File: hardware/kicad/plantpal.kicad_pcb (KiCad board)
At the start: 2 copper layers, 38.4 x 128.5 mm, 123 parts, among them J1 U262-161N-4BVC11, J2 +LIPO, J3 -LIPO, J4 687124182122, Q1 DMG1012UW, Q2 DMG3415U-7, Q3 MMBT3906, Q4 PMV32UP, Q5 DMG1012UW, Q6 AO3407A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

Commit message: update 3d model
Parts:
- D7, D8: footprint Diode_SMD:D_0402_1005Metric -> plantpal:D_0402_1005Metric
- Q8: footprint Package_TO_SOT_SMD:SOT-883 -> plantpal:SOT-883
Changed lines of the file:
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@@
     (property "ki_keywords" "capacitor cap")
     (attr smd)
-    (fp_text reference "C25" (at 1.755 -0.24 90) (layer "F.Fab")
+    (fp_text reference "C25" (at 1.505 0.29 90) (layer "F.Fab")
         (effects (font (size 0.3 0.3) (thickness 0.075) bold))
     )
@@
       (net 43 "Net-(J2-Pin_1)") (pinfunction "Pin_1") (pintype "passive"))
   )
-  (footprint "Package_TO_SOT_SMD:SOT-883" (layer "F.Cu")
+  (footprint "plantpal:SOT-883" (layer "F.Cu")
     (at 117.53 56.215 180)
     (descr "SOT-883, https://assets.nexperia.com/documents/outline-drawing/SOT883.pdf")
@@
     (property "ki_keywords" "transistor PMOS P-MOS P-MOSFET")
     (attr smd)
-    (fp_text reference "Q8" (at 0 -1.905) (layer "F.Fab")
+    (fp_text reference "Q8" (at -0.09 0.795 180) (layer "F.Fab")
         (effects (font (size 0.3 0.3) (thickness 0.075)))
     )
-    (fp_text value "PMZ350UPEYL" (at 0 1.905) (layer "F.Fab")
+    (fp_text value "PMZ350UPEYL" (at -2.16 0.895 180) (layer "F.Fab")
         (effects (font (size 0.3 0.3) (thickness 0.075)))
     )
-    (fp_text user "${REFERENCE}" (at 0 0) (layer "F.Fab")
+    (fp_text user "${REFERENCE}" (at 0 0 180) (layer "F.Fab")
         (effects (font (size 0.2 0.2) (thickness 0.03)))
     )
@@
     (pad "3" smd roundrect (at 0.35 0 180) (size 0.4 0.7) (layers "F.Cu" "F.Paste" "F.Mask") (roundrect_rratio 0.125)
       (net 89 "Net-(Q8-D)") (pinfunction "D") (pintype "passive"))
-    (model "${KICAD6_3DMODEL_DIR}/Package_TO_SOT_SMD.3dshapes/SOT-883.wrl"
+    (model "${KIPRJMOD}/library/3dmodels/X1-DFN1006-3_L1.0-W0.6-H0.5-P0.35-BR.wrl"
       (offset (xyz 0 0 0))
       (scale (xyz 1 1 1))
-      (rotate (xyz 0 0 0))
+      (rotate (xyz 0 0 180))
     )
   )
@@
     )
   )
-  (footprint "Diode_SMD:D_0402_1005Metric" (layer "F.Cu")
+  (footprint "plantpal:D_0402_1005Metric" (layer "F.Cu")
     (at 125.7825 37.06 180)
     (descr "Diode SMD 0402 (1005 Metric), square (rectangular) end terminal, IPC_7351 nominal, (Body size source: http://www.tortai-tech.com/upload/download/2011102023233369053.pdf), generated with kicad-footprint-generator")
@@
     (property "ki_keywords" "diode Schottky")
     (attr smd)
-    (fp_text reference "D8" (at 0 -1.17) (layer "F.Fab")
+    (fp_text reference "D8" (at -1.3475 -0.08 180) (layer "F.Fab")
         (effects (font (size 0.3 0.3) (thickness 0.075)))
     )
-    (fp_text value "RB161QS-40T18R" (at 0 1.17) (layer "F.Fab")
+    (fp_text value "RB161QS-40T18R" (at -0.9675 0.69 180) (layer "F.Fab")
         (effects (font (size 0.3 0.3) (thickness 0.075)))
     )
-    (fp_text user "${REFERENCE}" (at 0 0) (layer "F.Fab")
+    (fp_text user "${REFERENCE}" (at 0 0 180) (layer "F.Fab")
         (effects (font (size 0.25 0.25) (thickness 0.04)))
     )
@@
     (pad "2" smd roundrect (at 0.485 0 180) (size 0.59 0.64) (layers "F.Cu" "F.Paste" "F.Mask") (roundrect_rratio 0.25)
       (net 11 "/Main Controller/CHIP_EN") (pinfunction "A") (pintype "passive"))
-    (model "${KICAD6_3DMODEL_DIR}/Diode_SMD.3dshapes/D_0402_1005Metric.wrl"
+    (model "${KIPRJMOD}/library/3dmodels/X2-DFN1006-2_L1.0-W0.6-H0.4-P0.65-RD.wrl"
       (offset (xyz 0 0 0))
       (scale (xyz 1 1 1))
@@
     (property "ki_keywords" "R resistor")
     (attr smd)
-    (fp_text reference "R8" (at 0.81 0 90) (layer "F.Fab")
+    (fp_text reference "R8" (at 0.89 0.795 90) (layer "F.Fab")
         (effects (font (size 0.3 0.3) (thickness 0.075)))
     )
@@
     (property "ki_keywords" "R resistor")
     (attr smd)
-    (fp_text reference "R14" (at 0.06 -0.93 90) (layer "F.Fab")
+    (fp_text reference "R14" (at 0.23 -0.76 180) (layer "F.Fab")
         (effects (font (size 0.3 0.3) (thickness 0.075)))
     )
-    (fp_text value "16K9" (at 0.47 -0.93 90) (layer "F.Fab")
+    (fp_text value "16K9" (at 1.1 -1.59 -90) (layer "F.Fab")
         (effects (font (size 0.3 0.3) (thickness 0.075)))
     )
@@
     (property "ki_keywords" "capacitor cap")
     (attr smd)
-    (fp_text reference "C26" (at 1.735 0.24 90) (layer "F.Fab")
+    (fp_text reference "C26" (at -1.135 -0.7 180) (layer "F.Fab")
         (effects (font (size 0.3 0.3) (thickness 0.075)))
     )
-    (fp_text value "10u" (at 1.965 -0.57) (layer "F.Fab")
+    (fp_text value "10u" (at -1.105 0.99) (layer "F.Fab")
         (effects (font (size 0.3 0.3) (thickness 0.075)))
     )
@@
         (effects (font (size 0.3 0.3) (thickness 0.075)))
     )
-    (fp_text value "10K" (at 0 1.17) (layer "F.Fab")
+    (fp_text value "10K" (at -0.9 -0.72) (layer "F.Fab")
         (effects (font (size 0.3 0.3) (thickness 0.075)))
     )
@@
     (property "ki_keywords" "capacitor cap")
     (attr smd)
-    (fp_text reference "C13" (at -0.82 0 90) (layer "F.Fab")
+    (fp_text reference "C13" (at 0.48 0.675 180) (layer "F.Fab")
         (effects (font (size 0.3 0.3) (thickness 0.075)))
     )
@@
     (property "ki_keywords" "R resistor")
     (attr smd)
-    (fp_text reference "R28" (at 0 -1.17 90) (layer "F.Fab")
+    (fp_text reference "R28" (at -1.24 0.06 180) (layer "F.Fab")
         (effects (font (size 0.3 0.3) (thickness 0.075)))
     )
@@
     )
   )
-  (footprint "Diode_SMD:D_0402_1005Metric" (layer "F.Cu")
+  (footprint "plantpal:D_0402_1005Metric" (layer "F.Cu")
     (at 109.81 47.61 90)
     (descr "Diode SMD 0402 (1005 Metric), square (rectangular) end terminal, IPC_7351 nominal, (Body size source: http://www.tortai-tech.com/upload/download/2011102023233369053.pdf), generated with kicad-footprint-generator")
@@
     (property "ki_keywords" "diode Schottky")
     (attr smd)
-    (fp_text reference "D7" (at 0.74 0.8 180) (layer "F.Fab")
+    (fp_text reference "D7" (at 1.19 -0.35 180) (layer "F.Fab")
         (effects (font (size 0.3 0.3) (thickness 0.075)))
     )
-    (fp_text value "RB161QS-40T18R" (at 0.73 -0.61 270) (layer "F.Fab")
+    (fp_text value "RB161QS-40T18R" (at 0.77 2.67 180) (layer "F.Fab")
         (effects (font (size 0.3 0.3) (thickness 0.075)))
     )
@@
     (pad "2" smd roundrect (at 0.485 0 90) (size 0.59 0.64) (layers "F.Cu" "F.Paste" "F.Mask") (roundrect_rratio 0.25)
       (net 91 "/Main Controller/M_DRVOUT") (pinfunction "A") (pintype "passive"))
-    (model "${KICAD6_3DMODEL_DIR}/Diode_SMD.3dshapes/D_0402_1005Metric.wrl"
+    (model "${KIPRJMOD}/library/3dmodels/X2-DFN1006-2_L1.0-W0.6-H0.4-P0.65-RD.wrl"
       (offset (xyz 0 0 0))
       (scale (xyz 1 1 1))
@@
     (property "ki_keywords" "R resistor")
     (attr smd)
-    (fp_text reference "R9" (at 1.74 -0.355 180) (layer "F.Fab")
+    (fp_text reference "R9" (at 1.21 -0.095 -90) (layer "F.Fab")
         (effects (font (size 0.3 0.3) (thickness 0.075)))
     )

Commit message: wip
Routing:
- net /Main Controller/PWR_STATUS: track 8.65 -> 10.5 mm
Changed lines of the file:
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@@
   (via (at 127.92 60.15) (size 0.6) (drill 0.3) (layers "F.Cu" "B.Cu") (free) (net 2))
   (via (at 121.94 70.05) (size 0.6) (drill 0.3) (layers "F.Cu" "B.Cu") (free) (net 2))
-  (via (at 95.61 59.67) (size 0.6) (drill 0.3) (layers "F.Cu" "B.Cu") (free) (net 2))
+  (via (at 96.8 59.79) (size 0.6) (drill 0.3) (layers "F.Cu" "B.Cu") (free) (net 2))
   (via (at 100.96 70.08) (size 0.6) (drill 0.3) (layers "F.Cu" "B.Cu") (free) (net 2))
   (via (at 126.1 36.16) (size 0.6) (drill 0.3) (layers "F.Cu" "B.Cu") (free) (net 2))
@@
   (via (at 117.23 44.9) (size 0.6) (drill 0.3) (layers "F.Cu" "B.Cu") (net 2))
   (via (at 92.39 41.51) (size 0.6) (drill 0.3) (layers "F.Cu" "B.Cu") (free) (net 2))
+  (via (at 118.4 61.09) (size 0.6) (drill 0.3) (layers "F.Cu" "B.Cu") (free) (net 2))
   (via (at 100.93 67.63) (size 0.6) (drill 0.3) (layers "F.Cu" "B.Cu") (free) (net 2))
   (via (at 91.36 67.94) (size 0.6) (drill 0.3) (layers "F.Cu" "B.Cu") (free) (net 2))
@@
   (via (at 119.94 38.67) (size 0.6) (drill 0.3) (layers "F.Cu" "B.Cu") (free) (net 2))
   (via (at 116.26 47.86) (size 0.6) (drill 0.3) (layers "F.Cu" "B.Cu") (free) (net 2))
-  (via (at 97.96 60.7) (size 0.6) (drill 0.3) (layers "F.Cu" "B.Cu") (free) (net 2))
   (segment (start 115.505899 38.754) (end 115.503 38.754) (width 0.25) (layer "F.Cu") (net 4))
   (segment (start 113.92 37.845) (end 113.92 38.47) (width 0.6) (layer "F.Cu") (net 4))
@@
   (via (at 114.5 55.1) (size 0.6) (drill 0.3) (layers "F.Cu" "B.Cu") (net 58))
   (segment (start 110.01 54.9405) (end 110.01 56.451059) (width 0.25) (layer "B.Cu") (net 58))
+  (segment (start 112.6 53.39) (end 114.31 55.1) (width 0.25) (layer "B.Cu") (net 58))
+  (segment (start 110.54 53.39) (end 112.6 53.39) (width 0.25) (layer "B.Cu") (net 58))
+  (segment (start 110.01 53.92) (end 110.54 53.39) (width 0.25) (layer "B.Cu") (net 58))
   (segment (start 110.01 56.451059) (end 110.0095 56.451559) (width 0.25) (layer "B.Cu") (net 58))
-  (segment (start 110.1695 55.1) (end 110.01 54.9405) (width 0.25) (layer "B.Cu") (net 58))
-  (segment (start 114.5 55.1) (end 110.1695 55.1) (width 0.25) (layer "B.Cu") (net 58))
+  (segment (start 110.01 54.9405) (end 110.01 53.92) (width 0.25) (layer "B.Cu") (net 58))
+  (segment (start 114.31 55.1) (end 114.5 55.1) (width 0.25) (layer "B.Cu") (net 58))
   (segment (start 116.205 45.324) (end 116.196398 45.315398) (width 0.25) (layer "F.Cu") (net 59))
   (segment (start 115.28 52.14) (end 115.28 51.47) (width 0.5) (layer "F.Cu") (net 59))

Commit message: wip
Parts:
- moved C20 0.37 mm to (98.7, 51.9)
- moved R13 0.34 mm to (98.5, 49.9)
- turned D1 to 90 degrees
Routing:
- net +BATT: track 47.4 -> 46.6 mm
- net Net-(D1-K): track 6.70 -> 7.42 mm
- net GND: vias 188 -> 186

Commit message: wip
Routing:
- net GND: vias 186 -> 187
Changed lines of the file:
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@@
   (via (at 125.94 60.27) (size 0.6) (drill 0.3) (layers "F.Cu" "B.Cu") (free) (net 2))
   (via (at 111.44 39.17) (size 0.6) (drill 0.3) (layers "F.Cu" "B.Cu") (free) (net 2))
+  (via (at 99.83 48.17) (size 0.6) (drill 0.3) (layers "F.Cu" "B.Cu") (free) (net 2))
   (via (at 101.93 41.56) (size 0.6) (drill 0.3) (layers "F.Cu" "B.Cu") (free) (net 2))
   (via (at 110.96 40.55) (size 0.6) (drill 0.3) (layers "F.Cu" "B.Cu") (free) (net 2))

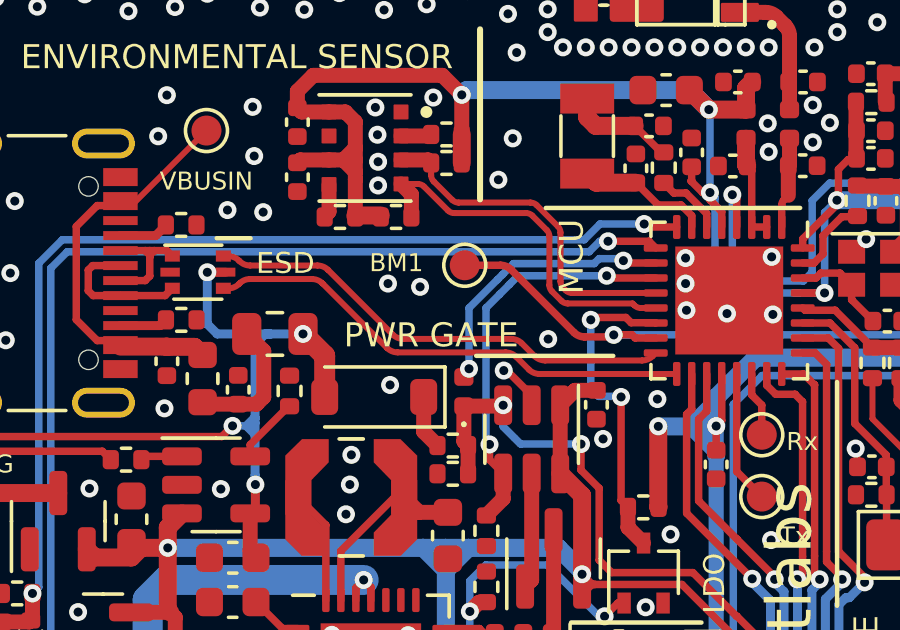
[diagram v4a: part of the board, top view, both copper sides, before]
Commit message: improve usb trace
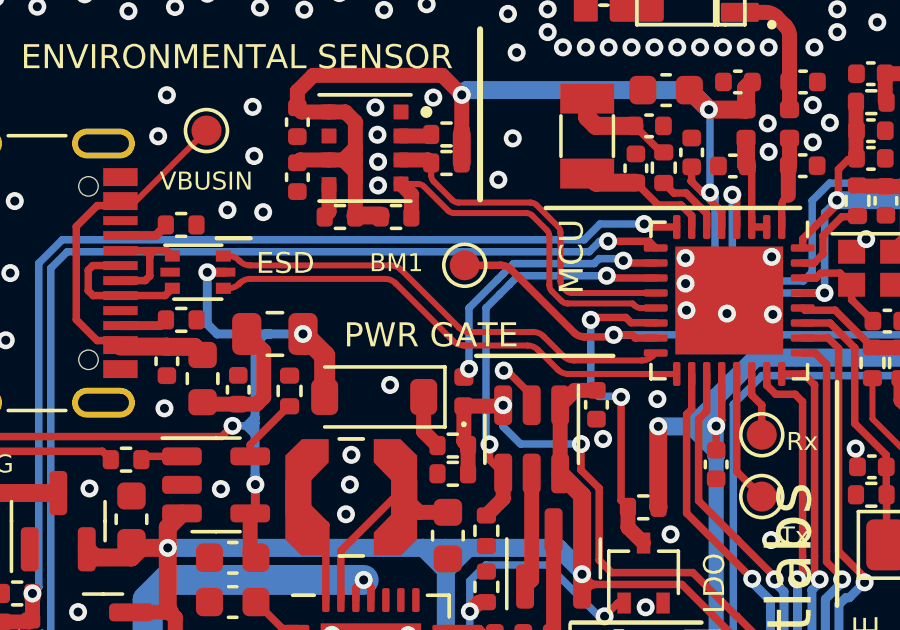
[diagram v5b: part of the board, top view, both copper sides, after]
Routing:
- net GND: vias 187 -> 184
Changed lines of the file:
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@@
   (via (at 128.03 67.67) (size 0.6) (drill 0.3) (layers "F.Cu" "B.Cu") (free) (net 2))
   (via (at 126.01 35.15) (size 0.6) (drill 0.3) (layers "F.Cu" "B.Cu") (free) (net 2))
-  (via (at 108.35 44.12) (size 0.6) (drill 0.3) (layers "F.Cu" "B.Cu") (free) (net 2))
   (via (at 97.88 71.55) (size 0.6) (drill 0.3) (layers "F.Cu" "B.Cu") (free) (net 2))
   (via (at 102.82 39.76) (size 0.6) (drill 0.3) (layers "F.Cu" "B.Cu") (free) (net 2))
@@
   (via (at 124.7 36.03) (size 0.6) (drill 0.3) (layers "F.Cu" "B.Cu") (free) (net 2))
   (via (at 126.27 72.15) (size 0.6) (drill 0.3) (layers "F.Cu" "B.Cu") (free) (net 2))
-  (via (at 112.62 45.86) (size 0.6) (drill 0.3) (layers "F.Cu" "B.Cu") (free) (net 2))
   (via (at 101.26 34.35) (size 0.6) (drill 0.3) (layers "F.Cu" "B.Cu") (free) (net 2))
   (via (at 98.09 65.78) (size 0.6) (drill 0.3) (layers "F.Cu" "B.Cu") (free) (net 2))
@@
   (via (at 102.19 33.67) (size 0.6) (drill 0.3) (layers "F.Cu" "B.Cu") (free) (net 2))
   (via (at 106.95 40.74) (size 0.6) (drill 0.3) (layers "F.Cu" "B.Cu") (free) (net 2))
-  (via (at 107.28 44.01) (size 0.6) (drill 0.3) (layers "F.Cu" "B.Cu") (free) (net 2))
   (via (at 92.46 34.42) (size 0.6) (drill 0.3) (layers "F.Cu" "B.Cu") (free) (net 2))
   (via (at 103.34 68.46) (size 0.6) (drill 0.3) (layers "F.Cu" "B.Cu") (free) (net 2))
@@
   (segment (start 119.74 48.06) (end 119.74 49.05) (width 0.25) (layer "F.Cu") (net 76))
   (segment (start 119.405 47.024) (end 119.405 47.725) (width 0.25) (layer "F.Cu") (net 76))
-  (segment (start 107.790307 45.855) (end 111.386093 45.855) (width 0.2) (layer "F.Cu") (net 77))
-  (segment (start 101.79 43.096) (end 101.957894 43.096) (width 0.2) (layer "F.Cu") (net 77))
-  (segment (start 112.519306 46.573999) (end 115.747894 46.573999) (width 0.2) (layer "F.Cu") (net 77))
-  (segment (start 102.684608 43.4085) (end 104.929593 43.4085) (width 0.2) (layer "F.Cu") (net 77))
+  (segment (start 102.687608 43.4045) (end 107.365593 43.4045) (width 0.2) (layer "F.Cu") (net 77))
+  (segment (start 112.469647 45.771447) (end 113.125753 46.427553) (width 0.2) (layer "F.Cu") (net 77))
+  (segment (start 113.479306 46.573999) (end 115.747894 46.573999) (width 0.2) (layer "F.Cu") (net 77))
+  (segment (start 110.000307 45.625) (end 112.116093 45.625) (width 0.2) (layer "F.Cu") (net 77))
+  (segment (start 101.793 43.092) (end 101.960894 43.092) (width 0.2) (layer "F.Cu") (net 77))
+  (segment (start 102.314448 43.238447) (end 102.334055 43.258054) (width 0.2) (layer "F.Cu") (net 77))
   (segment (start 116.101448 46.427552) (end 116.205 46.324) (width 0.2) (layer "F.Cu") (net 77))
-  (segment (start 111.739647 46.001447) (end 112.165753 46.427553) (width 0.2) (layer "F.Cu") (net 77))
-  (segment (start 105.283147 43.554947) (end 107.436754 45.708554) (width 0.2) (layer "F.Cu") (net 77))
-  (segment (start 102.311448 43.242447) (end 102.331055 43.262054) (width 0.2) (layer "F.Cu") (net 77))
-  (arc (start 102.684608 43.4085) (mid 102.493267 43.37044) (end 102.331055 43.262054) (width 0.2) (layer "F.Cu") (net 77))
-  (arc (start 101.957894 43.096) (mid 102.149236 43.13406) (end 102.311448 43.242447) (width 0.2) (layer "F.Cu") (net 77))
-  (arc (start 112.165753 46.427553) (mid 112.327965 46.535939) (end 112.519306 46.573999) (width 0.2) (layer "F.Cu") (net 77))
-  (arc (start 107.790307 45.855) (mid 107.598966 45.81694) (end 107.436754 45.708554) (width 0.2) (layer "F.Cu") (net 77))
-  (arc (start 111.386093 45.855) (mid 111.577435 45.89306) (end 111.739647 46.001447) (width 0.2) (layer "F.Cu") (net 77))
-  (arc (start 104.929593 43.4085) (mid 105.120935 43.44656) (end 105.283147 43.554947) (width 0.2) (layer "F.Cu") (net 77))
+  (segment (start 107.719147 43.550947) (end 109.646754 45.478554) (width 0.2) (layer "F.Cu") (net 77))
+  (arc (start 109.646754 45.478554) (mid 109.808966 45.58694) (end 110.000307 45.625) (width 0.2) (layer "F.Cu") (net 77))
+  (arc (start 102.334055 43.258054) (mid 102.496267 43.36644) (end 102.687608 43.4045) (width 0.2) (layer "F.Cu") (net 77))
   (arc (start 116.101448 46.427552) (mid 115.939236 46.535939) (end 115.747894 46.573999) (width 0.2) (layer "F.Cu") (net 77))
-  (segment (start 111.553247 46.451447) (end 111.979354 46.877554) (width 0.2) (layer "F.Cu") (net 78))
-  (segment (start 112.332907 47.024) (end 116.905 47.024) (width 0.2) (layer "F.Cu") (net 78))
-  (segment (start 101.79 44.171) (end 101.957894 44.171) (width 0.2) (layer "F.Cu") (net 78))
-  (segment (start 105.096747 44.004947) (end 107.250354 46.158554) (width 0.2) (layer "F.Cu") (net 78))
-  (segment (start 102.311448 44.024553) (end 102.331055 44.004946) (width 0.2) (layer "F.Cu") (net 78))
-  (segment (start 102.684608 43.8585) (end 104.743193 43.8585) (width 0.2) (layer "F.Cu") (net 78))
-  (segment (start 107.603907 46.305) (end 111.199693 46.305) (width 0.2) (layer "F.Cu") (net 78))
-  (arc (start 102.684608 43.8585) (mid 102.493267 43.89656) (end 102.331055 44.004946) (width 0.2) (layer "F.Cu") (net 78))
-  (arc (start 112.332907 47.024) (mid 112.141566 46.98594) (end 111.979354 46.877554) (width 0.2) (layer "F.Cu") (net 78))
-  (arc (start 107.250354 46.158554) (mid 107.412566 46.26694) (end 107.603907 46.305) (width 0.2) (layer "F.Cu") (net 78))
-  (arc (start 101.957894 44.171) (mid 102.149236 44.13294) (end 102.311448 44.024553) (width 0.2) (layer "F.Cu") (net 78))
-  (arc (start 111.553247 46.451447) (mid 111.391035 46.34306) (end 111.199693 46.305) (width 0.2) (layer "F.Cu") (net 78))
-  (arc (start 105.096747 44.004947) (mid 104.934535 43.89656) (end 104.743193 43.8585) (width 0.2) (layer "F.Cu") (net 78))
+  (arc (start 113.125753 46.427553) (mid 113.287965 46.535939) (end 113.479306 46.573999) (width 0.2) (layer "F.Cu") (net 77))
+  (arc (start 112.469647 45.771447) (mid 112.307435 45.66306) (end 112.116093 45.625) (width 0.2) (layer "F.Cu") (net 77))
+  (arc (start 102.314448 43.238447) (mid 102.152236 43.13006) (end 101.960894 43.092) (width 0.2) (layer "F.Cu") (net 77))
+  (arc (start 107.719147 43.550947) (mid 107.556935 43.44256) (end 107.365593 43.4045) (width 0.2) (layer "F.Cu") (net 77))
+  (segment (start 109.813907 46.075) (end 111.929693 46.075) (width 0.2) (layer "F.Cu") (net 78))
+  (segment (start 101.793 44.167) (end 101.960894 44.167) (width 0.2) (layer "F.Cu") (net 78))
+  (segment (start 102.314448 44.020553) (end 102.334055 44.000946) (width 0.2) (layer "F.Cu") (net 78))
+  (segment (start 107.532747 44.000947) (end 109.460354 45.928554) (width 0.2) (layer "F.Cu") (net 78))
+  (segment (start 113.292907 47.024) (end 116.905 47.024) (width 0.2) (layer "F.Cu") (net 78))
+  (segment (start 102.687608 43.8545) (end 107.179193 43.8545) (width 0.2) (layer "F.Cu") (net 78))
+  (segment (start 112.283247 46.221447) (end 112.939354 46.877554) (width 0.2) (layer "F.Cu") (net 78))
+  (arc (start 109.813907 46.075) (mid 109.622566 46.03694) (end 109.460354 45.928554) (width 0.2) (layer "F.Cu") (net 78))
+  (arc (start 111.929693 46.075) (mid 112.121035 46.11306) (end 112.283247 46.221447) (width 0.2) (layer "F.Cu") (net 78))
+  (arc (start 102.687608 43.8545) (mid 102.496267 43.89256) (end 102.334055 44.000946) (width 0.2) (layer "F.Cu") (net 78))
+  (arc (start 107.532747 44.000947) (mid 107.370535 43.89256) (end 107.179193 43.8545) (width 0.2) (layer "F.Cu") (net 78))
+  (arc (start 113.292907 47.024) (mid 113.101566 46.98594) (end 112.939354 46.877554) (width 0.2) (layer "F.Cu") (net 78))
+  (arc (start 101.960894 44.167) (mid 102.152236 44.12894) (end 102.314448 44.020553) (width 0.2) (layer "F.Cu") (net 78))
   (segment (start 110.33 55.51) (end 110.84 56.02) (width 0.25) (layer "F.Cu") (net 83))
   (segment (start 109.16 55.51) (end 110.33 55.51) (width 0.25) (layer "F.Cu") (net 83))
